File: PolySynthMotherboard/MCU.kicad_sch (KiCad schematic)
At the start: 13 parts, among them U201 STM32F411RETx, U202 74HC595, U203 74HC595

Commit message: motherboard hardware
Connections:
- net V5_CLK1: no longer U203.2 (QC)
- net V5_CLK2: no longer U203.3 (QD)
- net DAC_A0: now reaches U201.42 (PA9)
- net DAC_A1: now reaches U201.43 (PA10)
- net DAC_A2: now reaches U201.44 (PA11)
- net EXP_CS: now reaches U201.50 (PA15)
- net EXP_SCK: now reaches U201.51 (PC10)
- net EXP_MISO: now reaches U201.52 (PC11)
- net EXP_MOSI: now reaches U201.53 (PC12)
- net NRST: now reaches U201.7 (NRST)
- new net V6_CLK1: U203.2 (QC)
- new net V6_CLK2: U203.3 (QD)

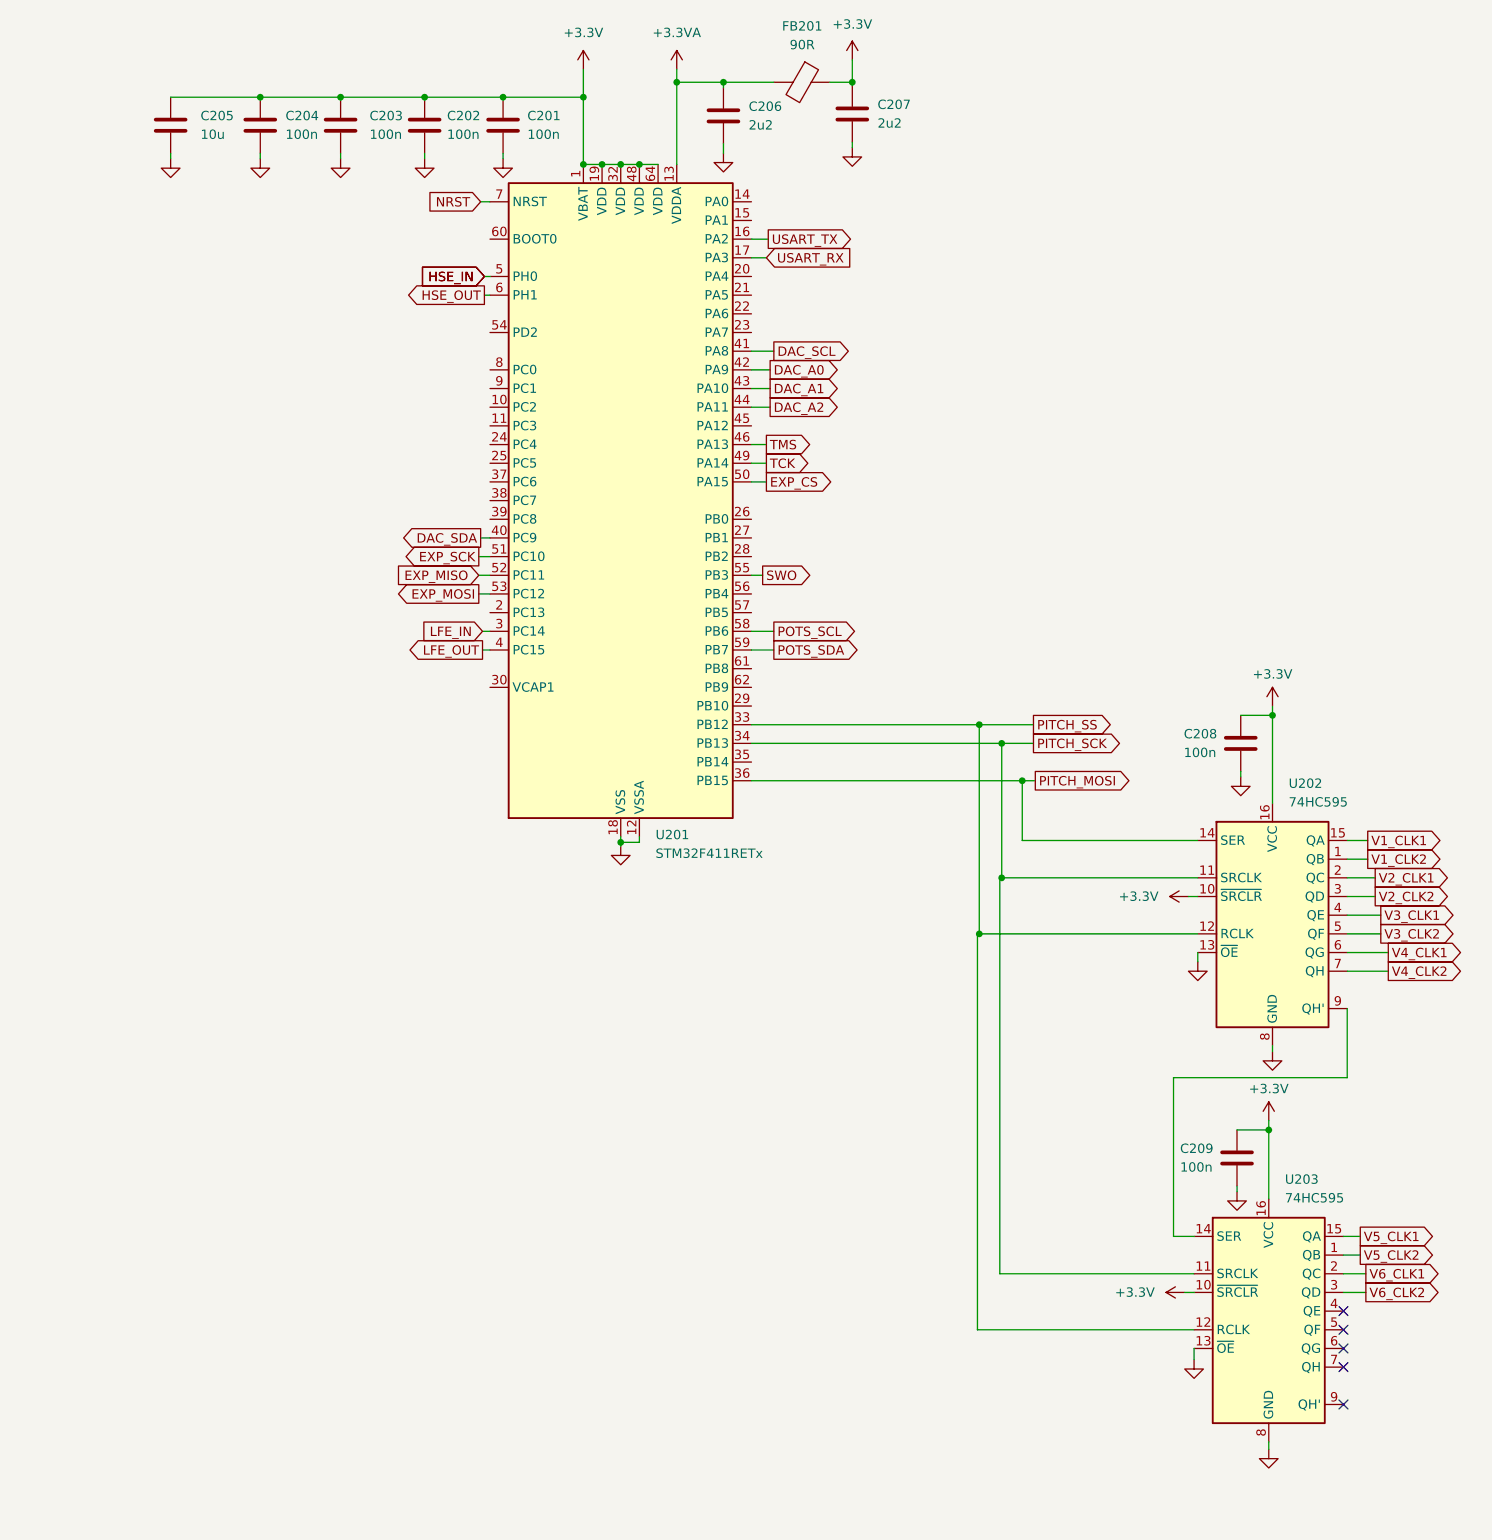
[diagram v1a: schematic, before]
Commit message: ioc for standalone F411
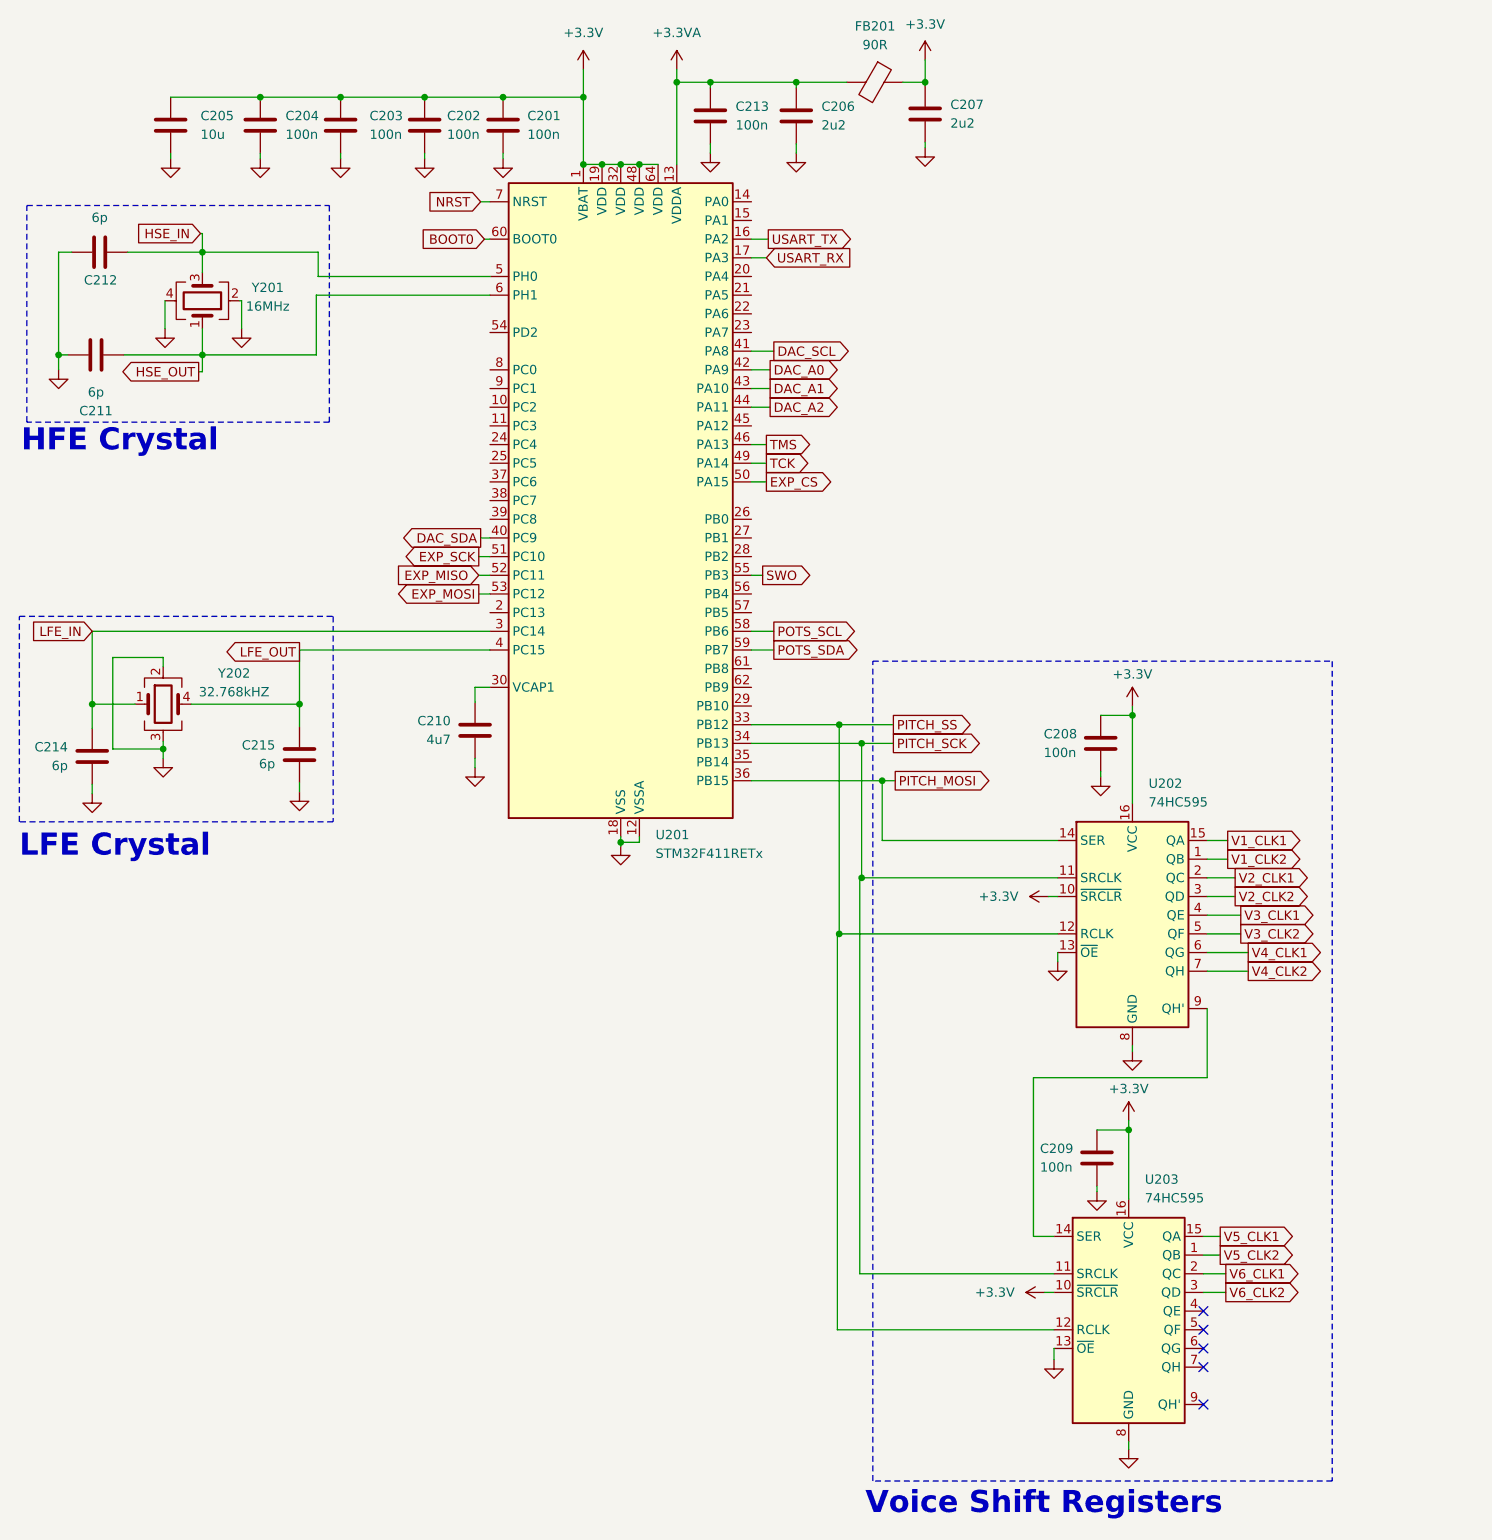
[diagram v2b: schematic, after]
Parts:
- added C210: 4u7, symbol Device:C
- added C211, C212: 6p, Capacitor_SMD:C_0805_2012Metric, symbol Device:C
- added C213: 100n, Capacitor_SMD:C_0805_2012Metric, symbol Device:C
- added C214, C215: 6p, symbol Device:C
- added Y201: 16MHz, Crystal:Crystal_SMD_EuroQuartz_MT-4Pin_3.2x2.5mm, symbol Device:Crystal_GND24
- added Y202: 32.768kHZ, symbol Device:Crystal_GND23
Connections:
- net +3.3VA: now also C213.1
- net GND: now also C210.2, C211.1, C212.1, C213.2, C214.2, C215.2, Y201.2, Y201.4, Y202.2, Y202.3
- net HSE_IN: now also C212.2, Y201.3
- net HSE_OUT: now also C211.2, Y201.1
- net LFE_IN: now also C214.1, Y202.1
- net LFE_OUT: now also C215.1, Y202.4
- net at U201.30 (VCAP1): now also C210.1
- net BOOT0: now reaches U201.60 (BOOT0)
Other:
- note added: "HFE Crystal"
- note added: "LFE Crystal"
- note added: "Voice Shift Registers"
- moved on the sheet: C206, C207, C208, C209, FB201, U202, U203

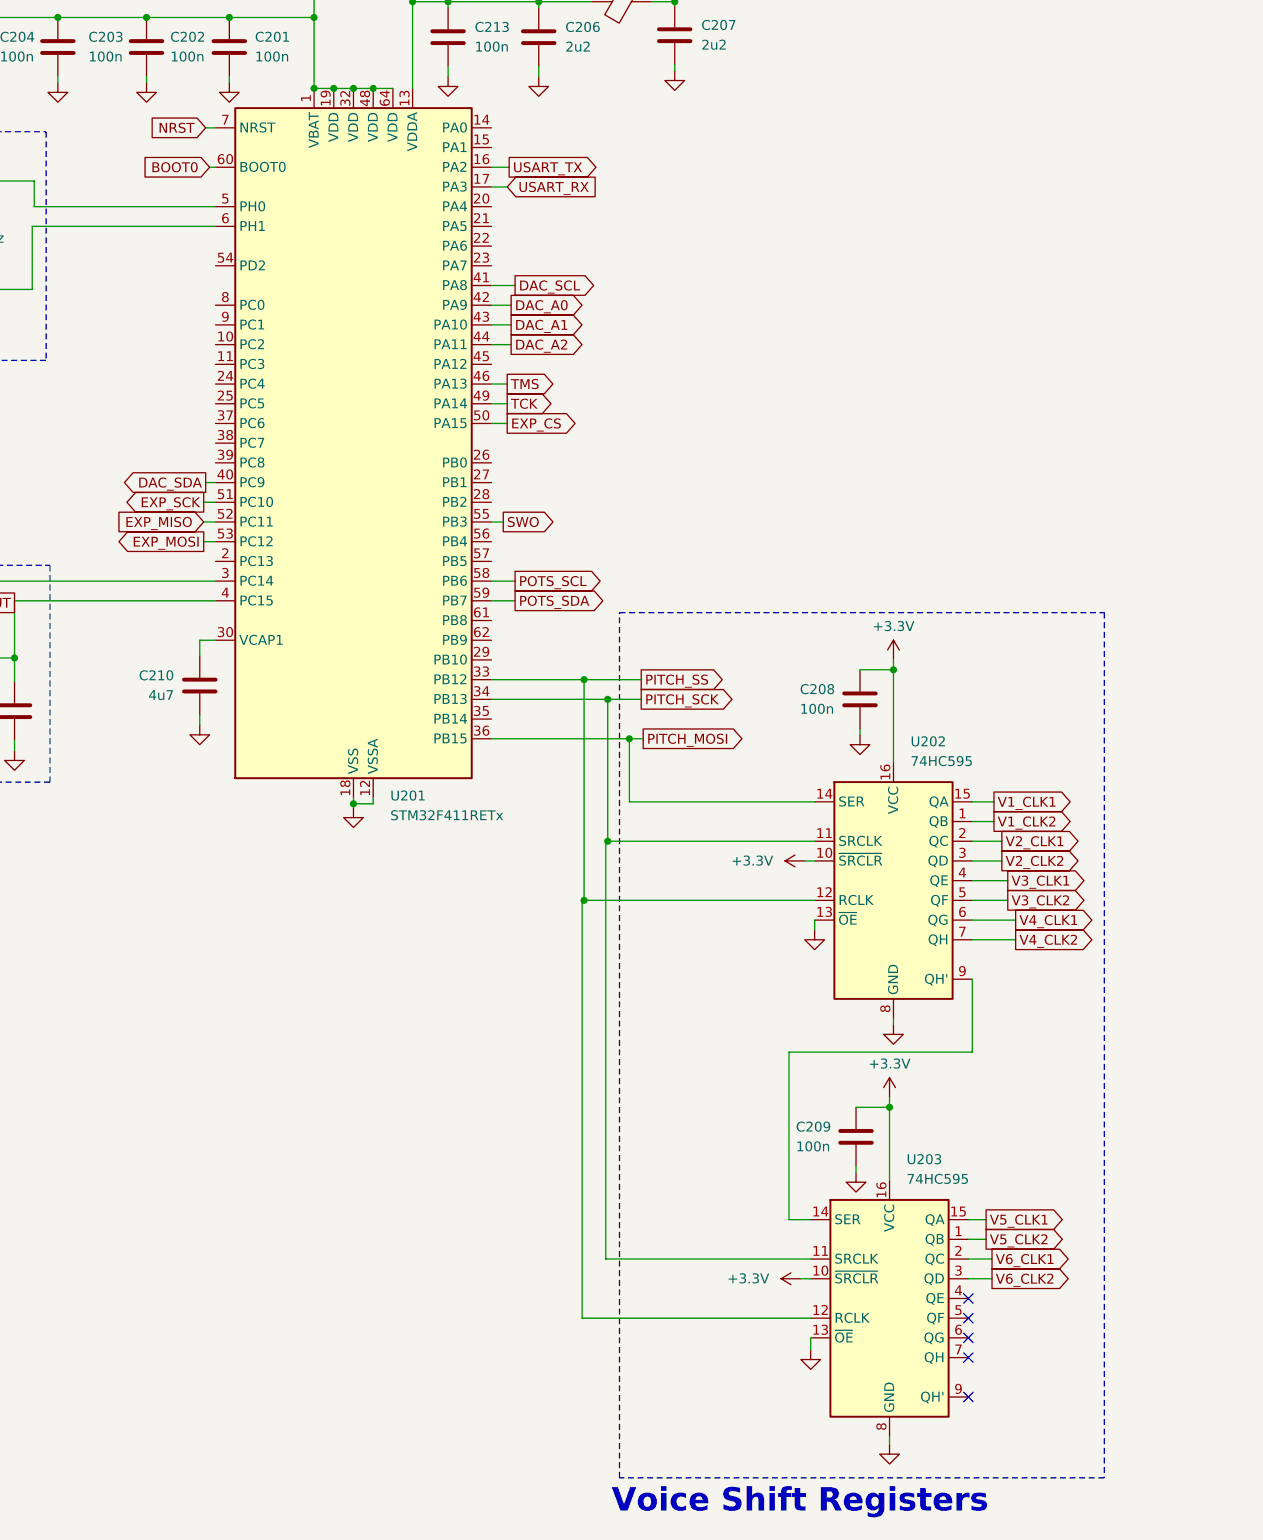
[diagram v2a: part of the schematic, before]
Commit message: fixed double buffering
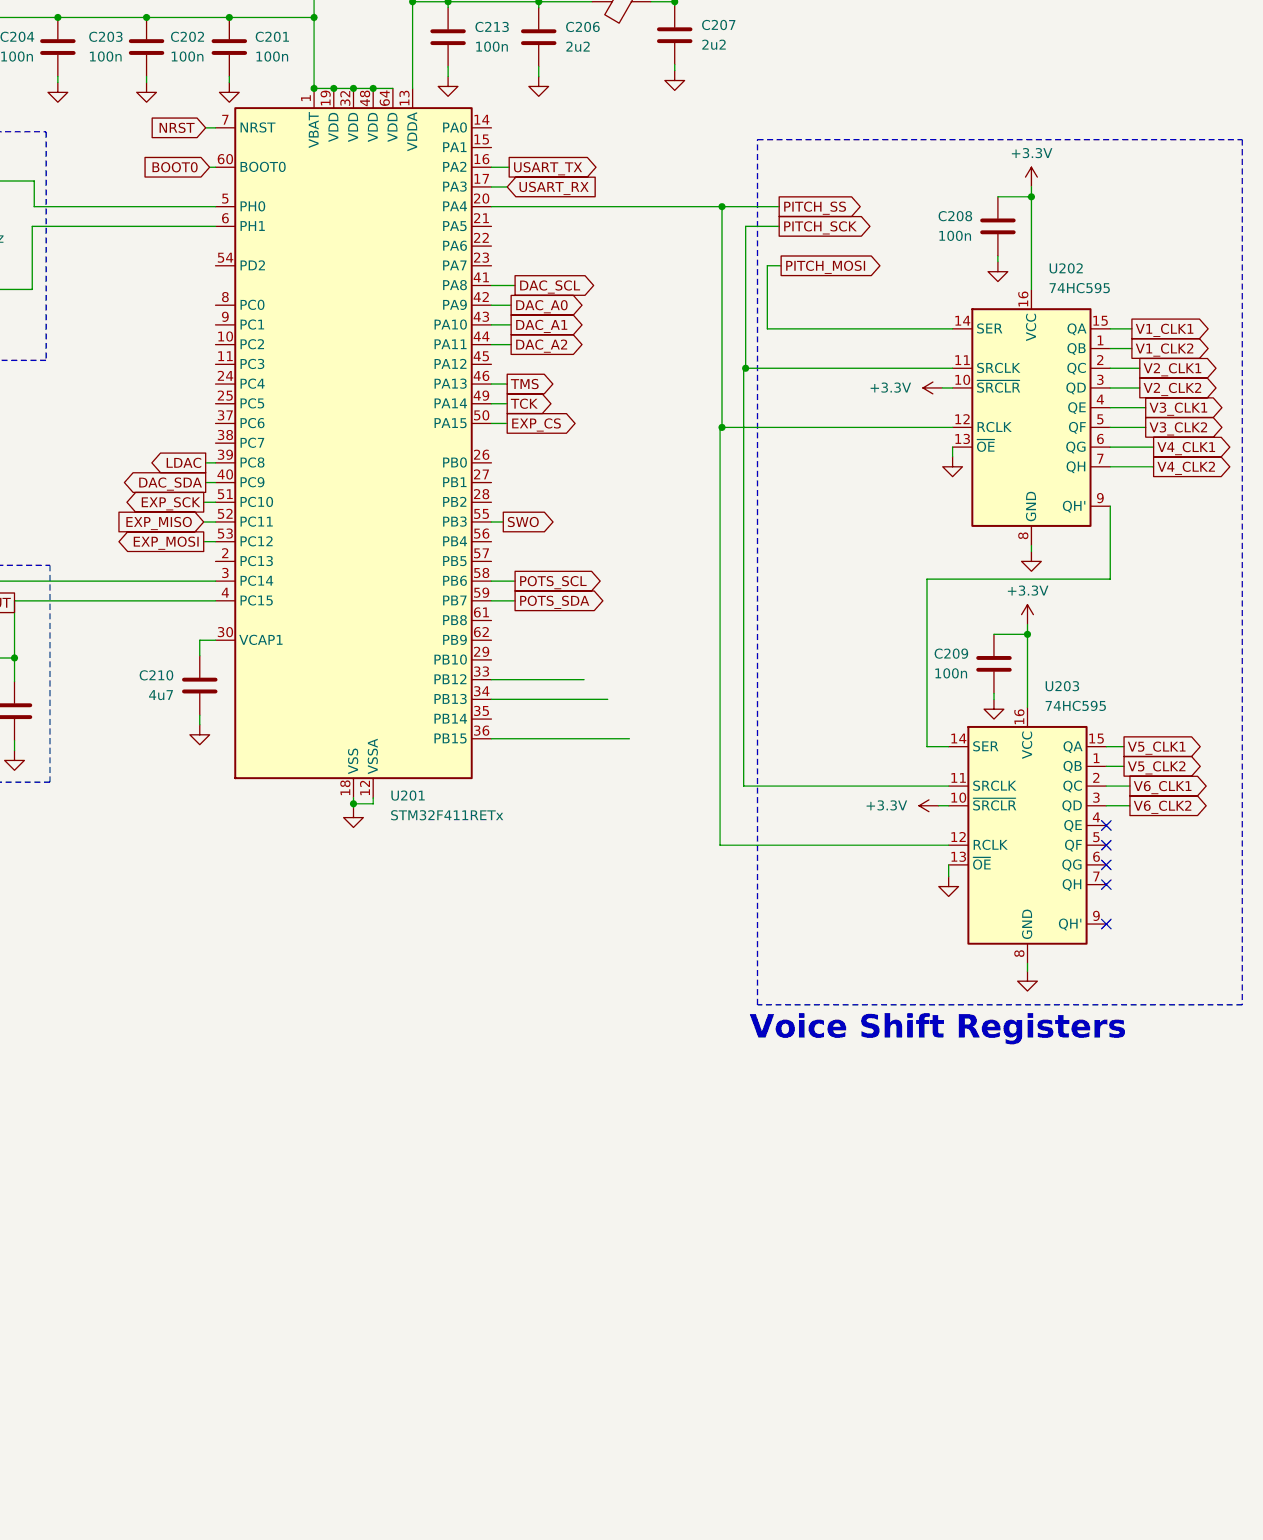
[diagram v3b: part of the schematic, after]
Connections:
- net PITCH_MOSI: no longer U201.36 (PB15)
- net PITCH_SCK: no longer U201.34 (PB13)
- net PITCH_SS: now also U201.20 (PA4); no longer U201.33 (PB12)
- net LDAC: now reaches U201.39 (PC8)
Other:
- moved on the sheet: C208, C209, U202, U203
